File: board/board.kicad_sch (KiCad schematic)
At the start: 3 parts, among them J1 001_I2C, J2 Conn_01x06_Male

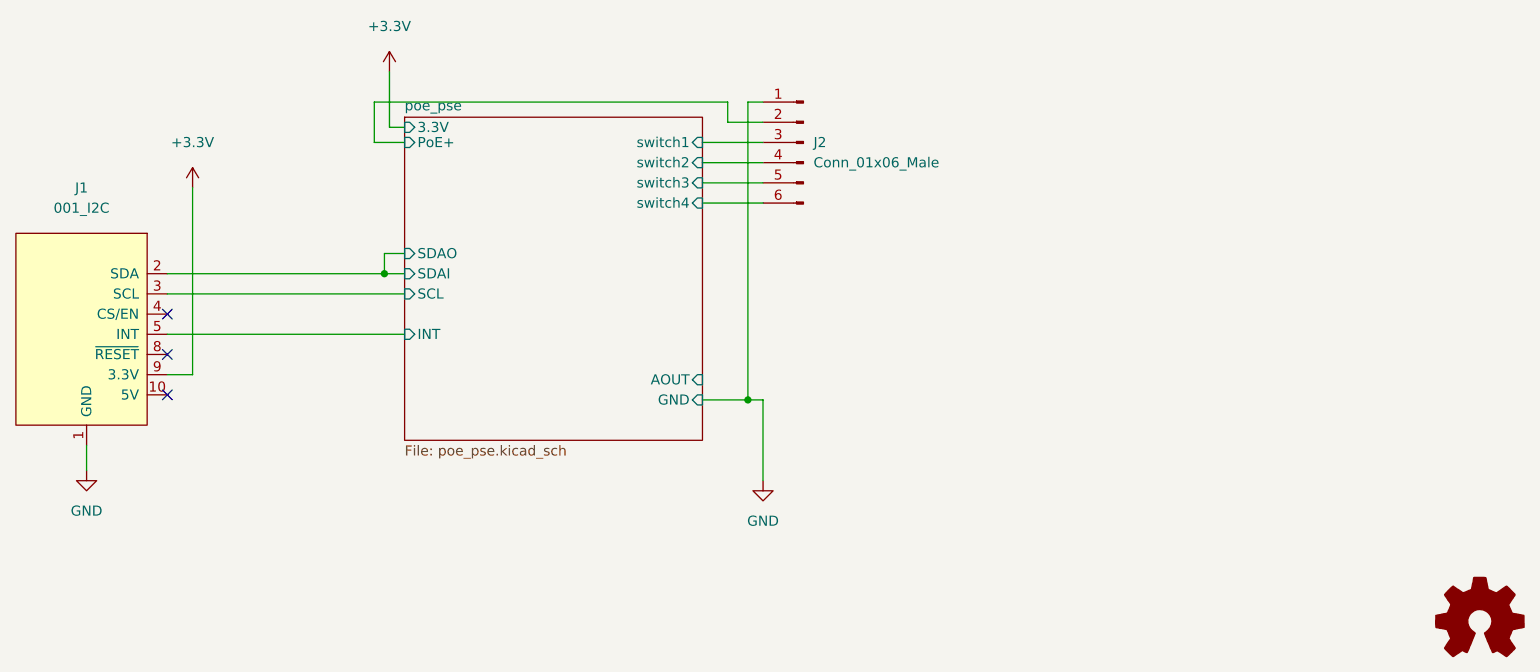
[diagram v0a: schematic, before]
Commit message: broke out address lines
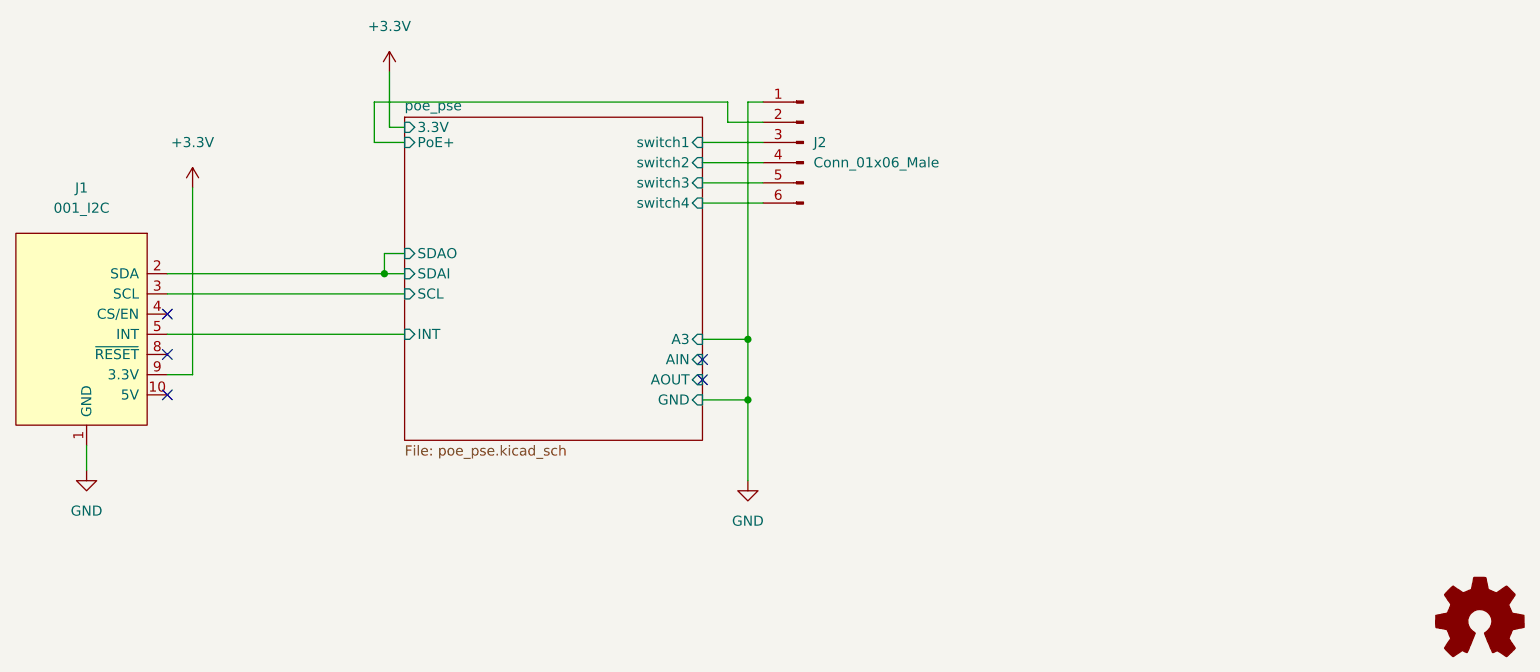
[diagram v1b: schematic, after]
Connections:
- no-connect marks 3 -> 5
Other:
- sheet poe_pse ports: added A3, AIN; removed none
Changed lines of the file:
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@@
   (junction (at 180.975 129.54) (diameter 0) (color 0 0 0 0)
   )
+  (junction (at 180.975 121.92) (diameter 0) (color 0 0 0 0)
+  )
   (junction (at 135.255 113.665) (diameter 0) (color 0 0 0 0)
   )
+  (no_connect (at 175.26 127))
+  (no_connect (at 175.26 124.46))
   (no_connect (at 107.95 118.745))
   (no_connect (at 107.95 123.825))
@@
     (stroke (width 0) (type default) (color 0 0 0 0))
   )
-  (wire (pts (xy 180.975 92.075) (xy 180.975 129.54))
+  (wire (pts (xy 180.975 92.075) (xy 180.975 121.92))
+    (stroke (width 0) (type default) (color 0 0 0 0))
+  )
+  (wire (pts (xy 175.26 121.92) (xy 180.975 121.92))
     (stroke (width 0) (type default) (color 0 0 0 0))
   )
@@
     (stroke (width 0) (type default) (color 0 0 0 0))
   )
-  (wire (pts (xy 182.88 129.54) (xy 182.88 139.7))
+  (wire (pts (xy 180.975 129.54) (xy 180.975 139.7))
     (stroke (width 0) (type default) (color 0 0 0 0))
   )
@@
     (stroke (width 0) (type default) (color 0 0 0 0))
   )
-  (wire (pts (xy 180.975 129.54) (xy 182.88 129.54))
-    (stroke (width 0) (type default) (color 0 0 0 0))
-  )
   (wire (pts (xy 175.26 102.235) (xy 182.88 102.235))
     (stroke (width 0) (type default) (color 0 0 0 0))
   )
   (wire (pts (xy 107.95 126.365) (xy 111.125 126.365))
+    (stroke (width 0) (type default) (color 0 0 0 0))
+  )
+  (wire (pts (xy 180.975 121.92) (xy 180.975 129.54))
     (stroke (width 0) (type default) (color 0 0 0 0))
   )
@@
     (pin "1")
   )
-  (symbol (lib_id "power:GND") (at 182.88 139.7 0) (unit 1)
-    (in_bom yes) (on_board yes) (fields_autoplaced)
-    (property "Reference" "#PWR0101" (id 0) (at 182.88 146.05 0)
-      (effects (font (size 1.27 1.27)) hide)
-    )
-    (property "Value" "GND" (id 1) (at 182.88 144.78 0))
-    (property "Footprint" "" (id 2) (at 182.88 139.7 0)
-      (effects (font (size 1.27 1.27)) hide)
-    )
-    (property "Datasheet" "" (id 3) (at 182.88 139.7 0)
+  (symbol (lib_id "power:GND") (at 180.975 139.7 0) (unit 1)
+    (in_bom yes) (on_board yes) (fields_autoplaced)
+    (property "Reference" "#PWR0101" (id 0) (at 180.975 146.05 0)
+      (effects (font (size 1.27 1.27)) hide)
+    )
+    (property "Value" "GND" (id 1) (at 180.975 144.78 0))
+    (property "Footprint" "" (id 2) (at 180.975 139.7 0)
+      (effects (font (size 1.27 1.27)) hide)
+    )
+    (property "Datasheet" "" (id 3) (at 180.975 139.7 0)
       (effects (font (size 1.27 1.27)) hide)
     )
@@
       (effects (font (size 1.27 1.27)) (justify left))
     )
-  )
+    (pin "AIN" input (at 175.26 124.46 0)
+      (effects (font (size 1.27 1.27)) (justify right))
+    )
+    (pin "A3" input (at 175.26 121.92 0)
+      (effects (font (size 1.27 1.27)) (justify right))
+    )
+  )

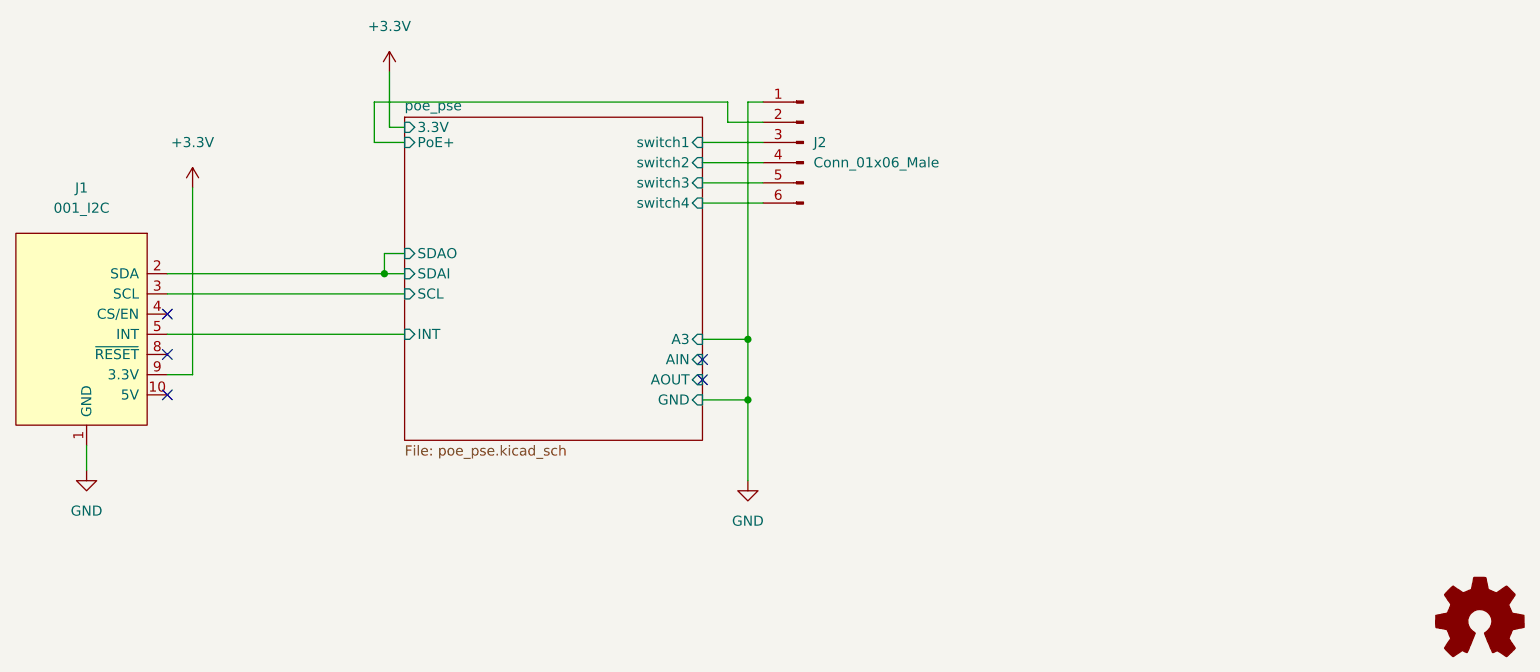
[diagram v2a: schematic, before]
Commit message: added lcsc part numbers
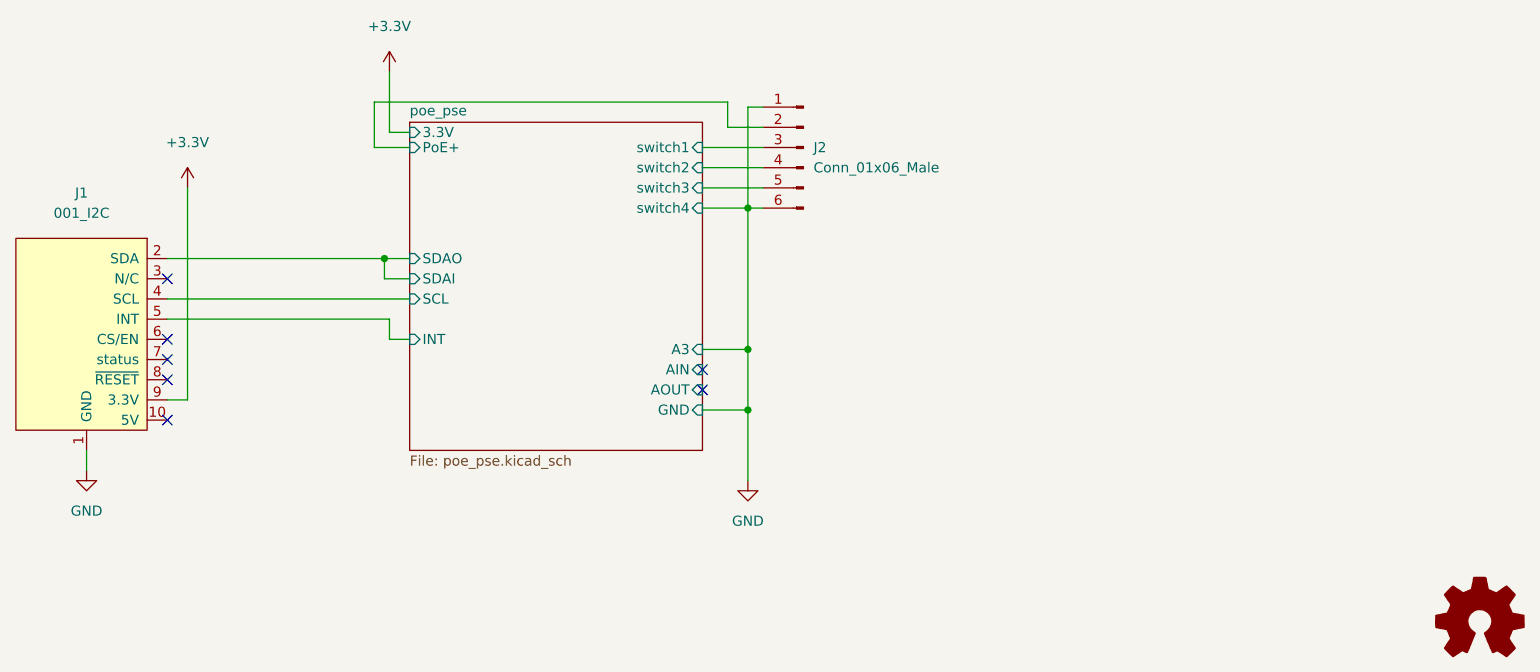
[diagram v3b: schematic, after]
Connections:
- net poe_pse/switch4 is gone; now on net GND: J2.6 (Pin_6)
- net poe_pse/SCL: now also J1.4 (SCL); no longer J1.3 (SCL)
- no-connect marks 5 -> 7
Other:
- moved on the sheet: J2
